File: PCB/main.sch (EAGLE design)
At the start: 52 parts, among them X1 BU-SMA-V

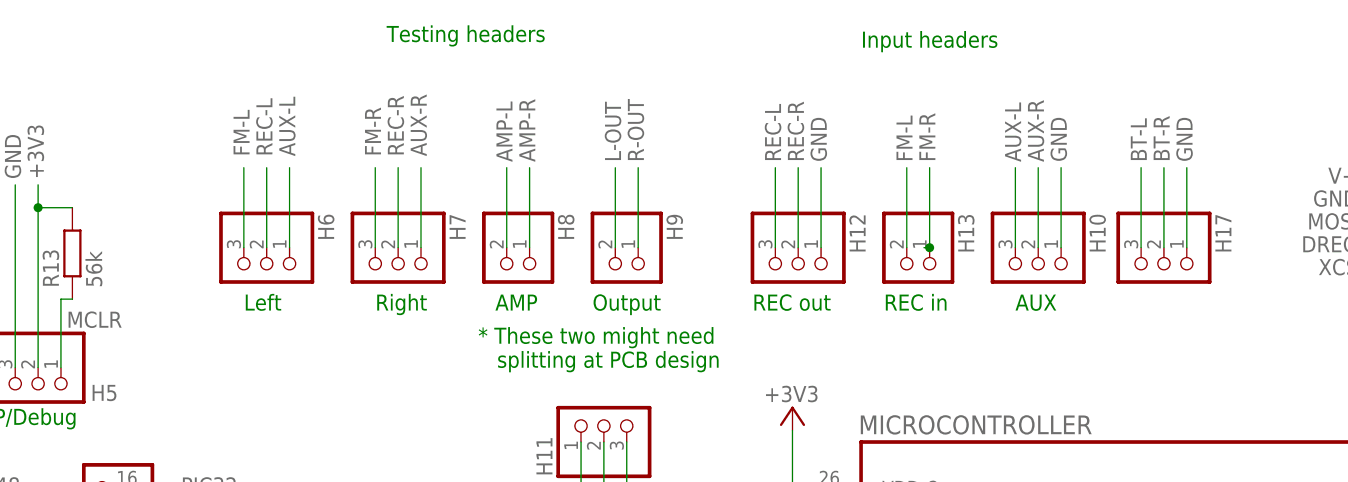
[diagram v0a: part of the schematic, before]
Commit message: Eagle Schematic Changes
Added BT to left and right test headers
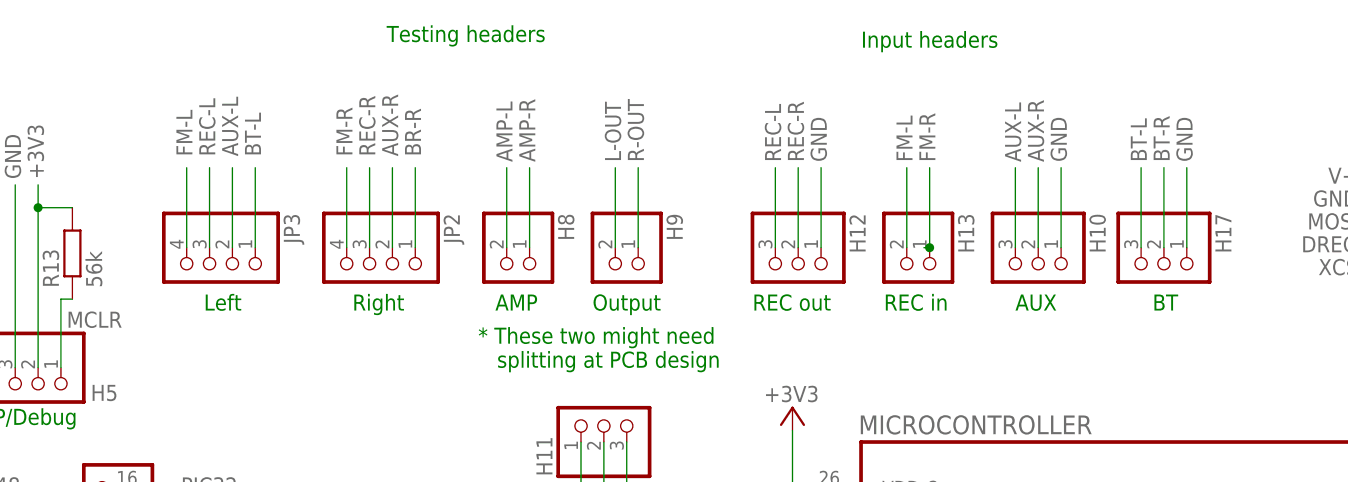
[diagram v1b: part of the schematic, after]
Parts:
- removed H6, H7: (no value), pinhead:PINHD-1X3
- added JP2, JP3: (no value), pinhead:PINHD-1X4/90
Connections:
- new net BR-R: JP2.1
- net AUX-L: now also JP3.2; no longer H6.1
- net AUX-R: now also JP2.2; no longer H7.1
- net BT-L: now also JP3.1
- net FM-L: now also JP3.4; no longer H6.3
- net FM-R: now also JP2.4; no longer H7.3
- net REC-L: now also JP3.3; no longer H6.2
- net REC-R: now also JP2.3; no longer H7.2
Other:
- note added: "BT"
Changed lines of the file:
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@@
 <part name="H13" library="pinhead" deviceset="PINHD-1X2" device=""/>
 <part name="H12" library="pinhead" deviceset="PINHD-1X3" device=""/>
-<part name="H6" library="pinhead" deviceset="PINHD-1X3" device=""/>
-<part name="H7" library="pinhead" deviceset="PINHD-1X3" device=""/>
 <part name="H8" library="pinhead" deviceset="PINHD-1X2" device=""/>
 <part name="H9" library="pinhead" deviceset="PINHD-1X2" device=""/>
@@
 <part name="JP1" library="pinhead" deviceset="PINHD-1X4" device="/90"/>
 <part name="H17" library="pinhead" deviceset="PINHD-1X3" device=""/>
+<part name="JP2" library="pinhead" deviceset="PINHD-1X4" device="/90"/>
+<part name="JP3" library="pinhead" deviceset="PINHD-1X4" device="/90"/>
 </parts>
 <sheets>
@@
 <text x="-19.685" y="126.365" size="1.778" layer="91">AMP </text>
 <text x="-8.89" y="126.365" size="1.778" layer="91">Output</text>
-<text x="-47.625" y="126.365" size="1.778" layer="91">Left</text>
-<text x="-33.02" y="126.365" size="1.778" layer="91">Right</text>
+<text x="-52.07" y="126.365" size="1.778" layer="91">Left</text>
+<text x="-35.56" y="126.365" size="1.778" layer="91">Right</text>
 <text x="-31.75" y="156.21" size="1.778" layer="91">Testing headers</text>
 <text x="20.955" y="155.575" size="1.778" layer="91">Input headers</text>
@@
 <text x="81.915" y="154.94" size="1.778" layer="91">Recorder</text>
 <text x="118.11" y="154.94" size="1.778" layer="91">Real Time Clock</text>
+<text x="53.34" y="126.365" size="1.778" layer="91">BT</text>
 </plain>
 <instances>
@@
 <instance part="H13" gate="G$1" x="26.035" y="130.81" rot="R270"/>
 <instance part="H12" gate="A" x="13.97" y="130.81" rot="R270"/>
-<instance part="H6" gate="A" x="-45.085" y="130.81" rot="R270"/>
-<instance part="H7" gate="A" x="-30.48" y="130.81" rot="R270"/>
 <instance part="H8" gate="G$1" x="-18.415" y="130.81" rot="R270"/>
 <instance part="H9" gate="G$1" x="-6.35" y="130.81" rot="R270"/>
@@
 <instance part="JP1" gate="A" x="125.095" y="127" rot="R270"/>
 <instance part="H17" gate="A" x="54.61" y="130.81" rot="R270"/>
+<instance part="JP2" gate="A" x="-33.655" y="130.81" rot="R270"/>
+<instance part="JP3" gate="A" x="-51.435" y="130.81" rot="R270"/>
 </instances>
 <busses>
@@
 </segment>
 <segment>
-<wire x1="-45.085" y1="133.35" x2="-45.085" y2="142.24" width="0.1524" layer="91"/>
-<label x="-44.45" y="143.51" size="1.778" layer="95" rot="R90"/>
-<pinref part="H6" gate="A" pin="2"/>
+<wire x1="-51.435" y1="133.35" x2="-51.435" y2="142.24" width="0.1524" layer="91"/>
+<label x="-50.8" y="143.51" size="1.778" layer="95" rot="R90"/>
+<pinref part="JP3" gate="A" pin="3"/>
 </segment>
 <segment>
@@
 </segment>
 <segment>
-<wire x1="-42.545" y1="133.35" x2="-42.545" y2="142.24" width="0.1524" layer="91"/>
-<label x="-41.91" y="143.51" size="1.778" layer="95" rot="R90"/>
-<pinref part="H6" gate="A" pin="1"/>
+<wire x1="-48.895" y1="133.35" x2="-48.895" y2="142.24" width="0.1524" layer="91"/>
+<label x="-48.26" y="143.51" size="1.778" layer="95" rot="R90"/>
+<pinref part="JP3" gate="A" pin="2"/>
 </segment>
 <segment>
@@
 </segment>
 <segment>
-<wire x1="-33.02" y1="133.35" x2="-33.02" y2="142.24" width="0.1524" layer="91"/>
-<label x="-32.385" y="143.51" size="1.778" layer="95" rot="R90"/>
-<pinref part="H7" gate="A" pin="3"/>
+<wire x1="-36.195" y1="133.35" x2="-36.195" y2="142.24" width="0.1524" layer="91"/>
+<label x="-35.56" y="143.51" size="1.778" layer="95" rot="R90"/>
+<pinref part="JP2" gate="A" pin="4"/>
 </segment>
 <segment>
@@
 </segment>
 <segment>
-<wire x1="-47.625" y1="133.35" x2="-47.625" y2="142.24" width="0.1524" layer="91"/>
-<label x="-46.99" y="143.51" size="1.778" layer="95" rot="R90"/>
-<pinref part="H6" gate="A" pin="3"/>
+<wire x1="-53.975" y1="133.35" x2="-53.975" y2="142.24" width="0.1524" layer="91"/>
+<label x="-53.34" y="143.51" size="1.778" layer="95" rot="R90"/>
+<pinref part="JP3" gate="A" pin="4"/>
 </segment>
 <segment>
@@
 </segment>
 <segment>
-<wire x1="-30.48" y1="133.35" x2="-30.48" y2="142.24" width="0.1524" layer="91"/>
-<label x="-29.845" y="143.51" size="1.778" layer="95" rot="R90"/>
-<pinref part="H7" gate="A" pin="2"/>
+<wire x1="-33.655" y1="133.35" x2="-33.655" y2="142.24" width="0.1524" layer="91"/>
+<label x="-33.02" y="143.51" size="1.778" layer="95" rot="R90"/>
+<pinref part="JP2" gate="A" pin="3"/>
 </segment>
 <segment>
@@
 </segment>
 <segment>
-<wire x1="-27.94" y1="133.35" x2="-27.94" y2="142.24" width="0.1524" layer="91"/>
-<label x="-27.305" y="143.51" size="1.778" layer="95" rot="R90"/>
-<pinref part="H7" gate="A" pin="1"/>
+<wire x1="-31.115" y1="133.35" x2="-31.115" y2="142.24" width="0.1524" layer="91"/>
+<label x="-30.48" y="143.51" size="1.778" layer="95" rot="R90"/>
+<pinref part="JP2" gate="A" pin="2"/>
 </segment>
 <segment>
@@
 <label x="155.575" y="30.48" size="1.778" layer="95" rot="R180"/>
 </segment>
+<segment>
+<pinref part="JP3" gate="A" pin="1"/>
+<wire x1="-46.355" y1="133.35" x2="-46.355" y2="142.24" width="0.1524" layer="91"/>
+<label x="-45.72" y="143.51" size="1.778" layer="95" rot="R90"/>
+</segment>
 </net>
 <net name="BT-R" class="0">
@@
 </segment>
 </net>
+<net name="BR-R" class="0">
+<segment>
+<pinref part="JP2" gate="A" pin="1"/>
+<wire x1="-28.575" y1="133.35" x2="-28.575" y2="142.24" width="0.1524" layer="91"/>
+<label x="-27.94" y="143.51" size="1.778" layer="95" rot="R90"/>
+</segment>
+</net>

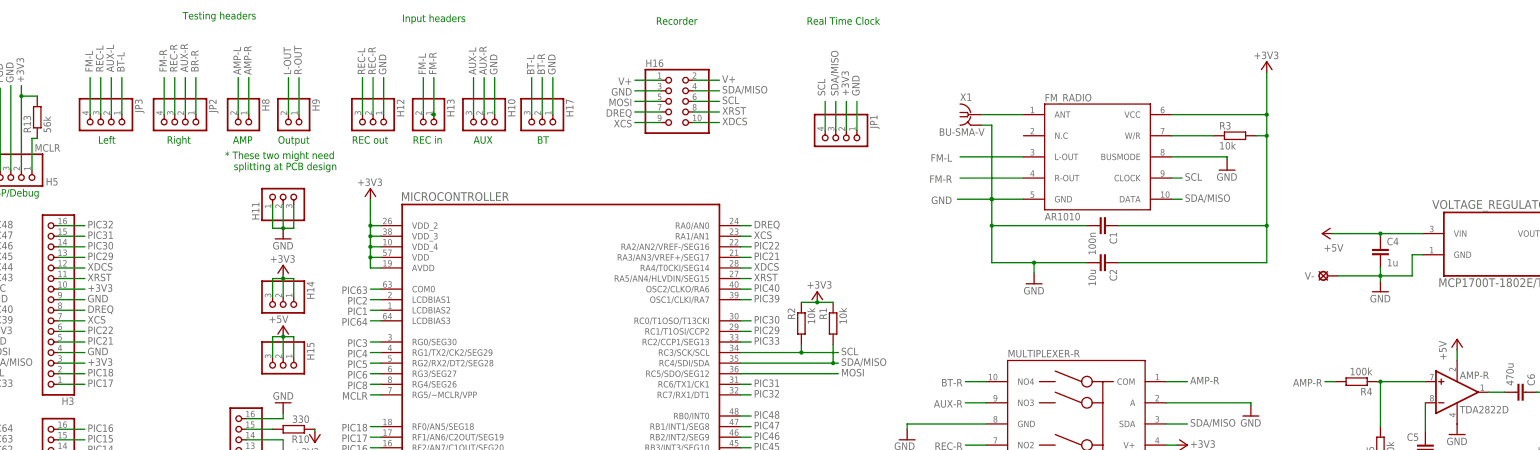
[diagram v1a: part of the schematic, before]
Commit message: Eagle Schematic Changes
Simple layout and naming changes
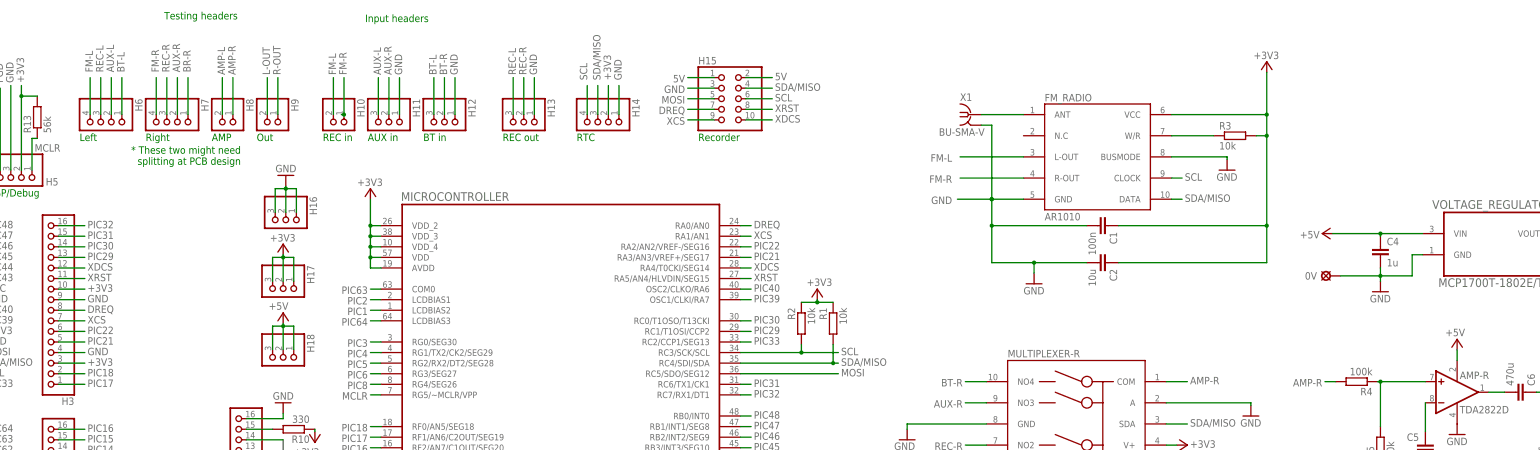
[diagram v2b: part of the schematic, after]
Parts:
- removed JP1, JP2: (no value), pinhead:PINHD-1X4/90
- removed V-: LSP11, solpad:LSP11
- added 0V: LSP11, solpad:LSP11
- added H18: (no value), pinhead:PINHD-1X3
- added H7: (no value), pinhead:PINHD-1X4/90
- H10: device pinhead:PINHD-1X3 -> pinhead:PINHD-1X2
- H13: device pinhead:PINHD-1X2 -> pinhead:PINHD-1X3
- H14: device pinhead:PINHD-1X3 -> pinhead:PINHD-1X4/90
- H15: device pinhead:PINHD-1X3 -> pinhead:PINHD-2X5
- H16: device pinhead:PINHD-2X5 -> pinhead:PINHD-1X3
- renumbered JP3 to H6
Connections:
- removed net V+: H16.1, H16.2
- new net 5V: H15.1, H15.2
- net +3V3: now also H17.1, H17.2, H17.3; no longer H14.1, H14.3, JP1.2
- net +5V: now also H18.1, H18.2, H18.3; no longer H15.1, H15.2, H15.3
- net AUX-L: now also H11.3; no longer H10.3
- net AUX-R: now also H11.2, H7.2; no longer H10.2, JP2.2
- net BR-R: now also H7.1; no longer JP2.1
- net BT-L: now also H12.3; no longer H17.3
- net BT-R: now also H12.2; no longer H17.2
- net DREQ: now also H15.7; no longer H16.7
- net FM-L: now also H10.2; no longer H13.2
- net FM-R: now also H10.1, H7.4; no longer H13.1, JP2.4
- net GND: now also 0V.MP, H13.1, H14.1, H15.3, H16.1, H16.2; no longer H10.1, H11.2, H11.3, H17.1, JP1.1, V-.MP
- net MOSI: now also H15.5; no longer H16.5
- net REC-L: now also H13.3; no longer H12.3
- net REC-R: now also H13.2, H7.3; no longer H12.2, JP2.3
- net SCL: now also H14.4, H15.6; no longer H16.6, JP1.4
- net SDA/MISO: now also H14.3, H15.4; no longer H16.4, JP1.3
- net XCS: now also H15.9; no longer H16.9
- net XDCS: now also H15.10; no longer H16.10
- net XRST: now also H15.8; no longer H16.8
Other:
- note added: "AUX in"
- note added: "BT in"
- note added: "Out"
- note added: "RTC"
- note removed: "AUX"
- note removed: "BT"
- note removed: "Output"
- note removed: "Real Time Clock"
- moved on the sheet: H11, H12, H17, H8, H9
